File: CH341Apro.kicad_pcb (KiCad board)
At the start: 2 copper layers, 27.5 x 69 mm, 18 parts, among them J1 USB_A, J3 ZIF-16, J4 , J5 V_SEL, U1 AMS1117-3.3, U2 CH341a, Y1 12M

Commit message: Add JLCPCB assembly infos
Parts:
- removed R2: 0R, Resistor_SMD:R_0805_2012Metric
- removed REF**: WEEE-Logo_4.2x6mm_SilkScreen, Symbol:WEEE-Logo_4.2x6mm_SilkScreen
- added JP1: , Jumper:SolderJumper-2_P1.3mm_Open_Pad1.0x1.5mm, F.Cu at (109.2, 99.1)
- C5, C6: footprint Capacitor_SMD:C_0603_1608Metric -> Capacitor_SMD:C_0402_1005Metric
- R1: footprint Resistor_SMD:R_0805_2012Metric -> Resistor_SMD:R_0603_1608Metric
- Y1: footprint Crystal:Crystal_HC49-4H_Vertical -> Crystal:Crystal_SMD_5032-2Pin_5.0x3.2mm
- moved C6 2.87 mm to (114.2, 95.2), turned to 270 degrees
- moved C5 2.84 mm to (114.2, 87.0), turned to 90 degrees
- moved Y1 2.48 mm to (114.2, 91.2)
- moved R1 0.14 mm to (110.7, 105.5)
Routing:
- net /3V3: track 84.3 -> 89.5 mm
- net Net-(C3-Pad2): track 17.9 -> 14.1 mm
- net Net-(C5-Pad1): track 13.6 -> 10.2 mm
- net Net-(C6-Pad1): track 9.38 -> 6.58 mm
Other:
- rule pad_to_mask_clearance: 0.05 -> 0

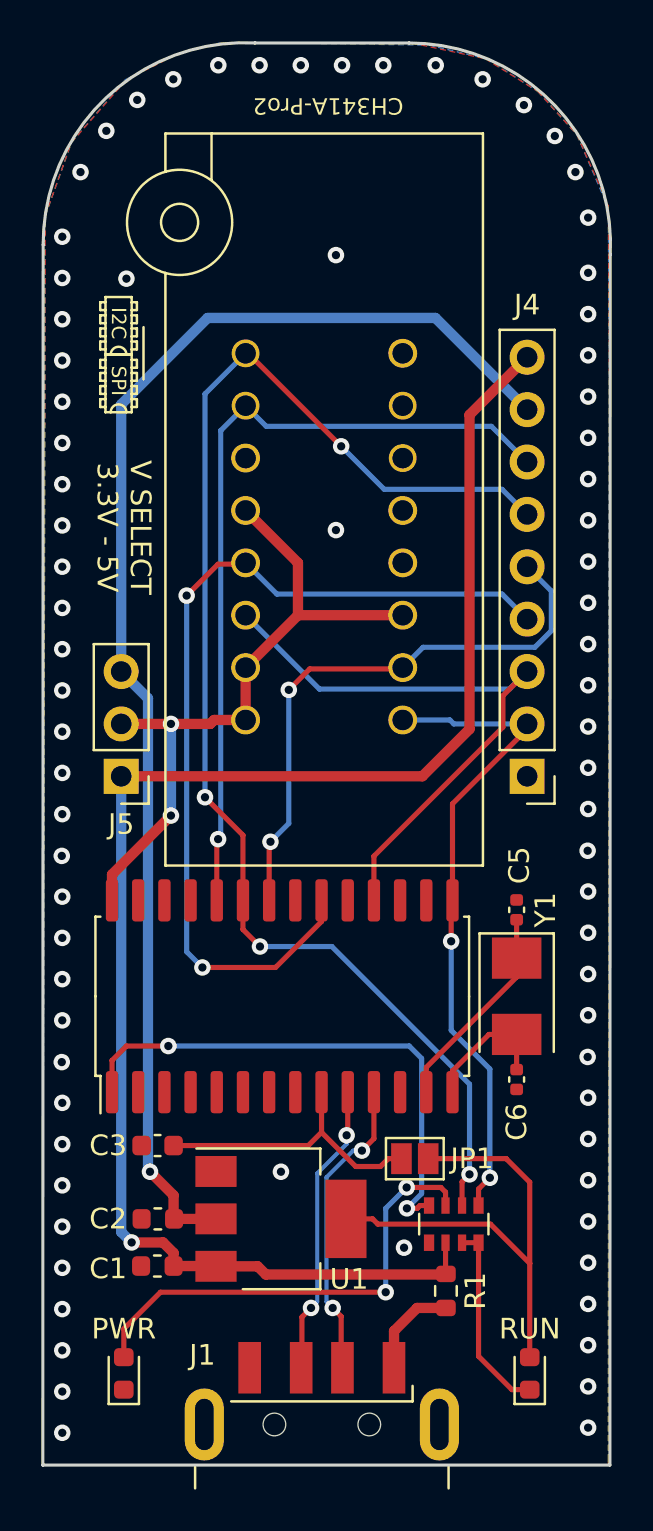
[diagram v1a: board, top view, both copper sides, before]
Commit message: Major ergo change
Updated components footprints for hand soldering.
Change VCC routing.
Add JP1/2 for selecting operating voltage.
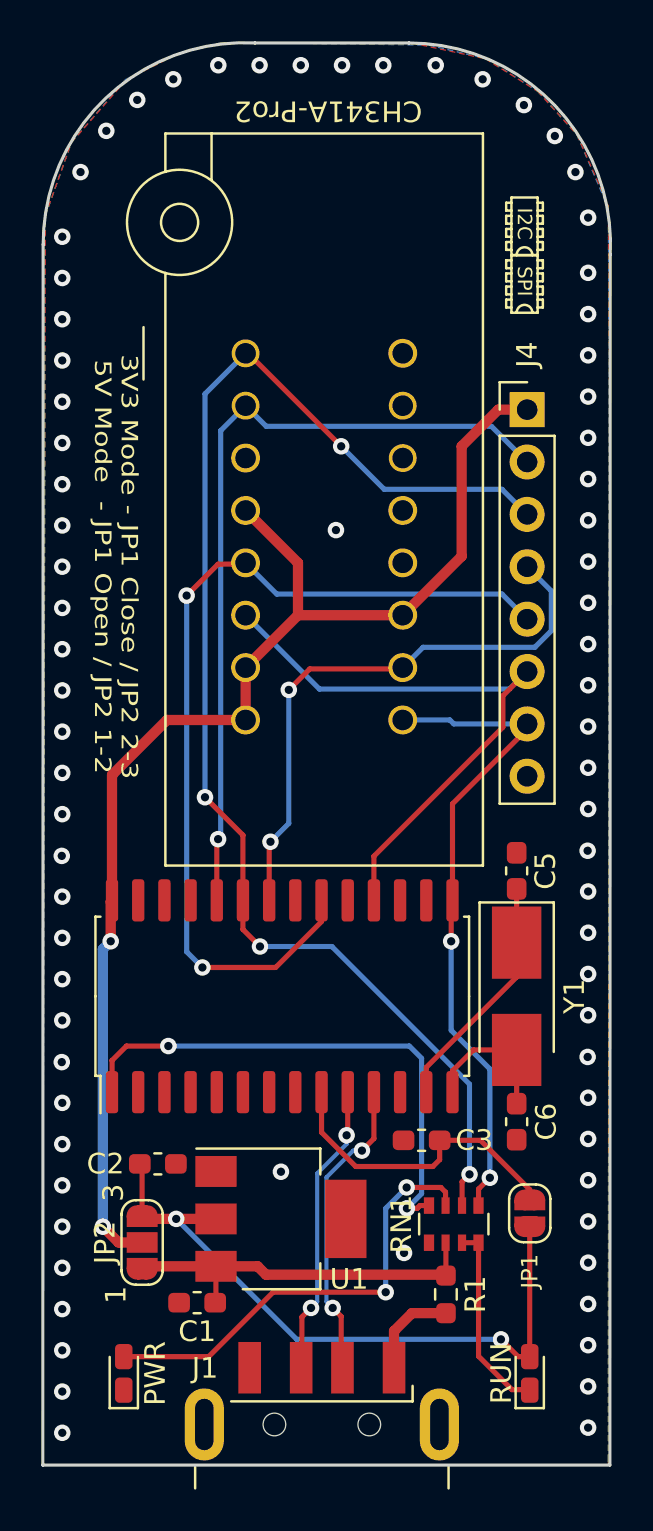
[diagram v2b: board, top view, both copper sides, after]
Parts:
- removed D1: PWR, LED_SMD:LED_0603_1608Metric
- removed D2: RUN, LED_SMD:LED_0603_1608Metric
- removed J5: V_SEL, Connector_PinHeader_2.54mm:PinHeader_1x03_P2.54mm_Vertical
- added JP2: V_SEL, Jumper:SolderJumper-3_P1.3mm_Open_RoundedPad1.0x1.5mm_NumberLabels, F.Cu at (96.0, 103.1)
- added PWR: PWR, LED_SMD:LED_0603_1608Metric_Castellated, F.Cu at (95.1, 109.5)
- added RUN: RUN, LED_SMD:LED_0603_1608Metric_Castellated, F.Cu at (114.8, 109.5)
- C1, C2, C3: footprint Capacitor_SMD:C_0603_1608Metric -> Capacitor_SMD:C_0603_1608Metric_Pad1.05x0.95mm_HandSolder
- C5, C6: footprint Capacitor_SMD:C_0402_1005Metric -> Capacitor_SMD:C_0603_1608Metric_Pad1.05x0.95mm_HandSolder
- J4: footprint Connector_PinHeader_2.54mm:PinHeader_1x09_P2.54mm_Vertical -> Connector_PinHeader_2.54mm:PinHeader_1x08_P2.54mm_Vertical
- JP1: footprint Jumper:SolderJumper-2_P1.3mm_Open_Pad1.0x1.5mm -> Jumper:SolderJumper-2_P1.3mm_Open_RoundedPad1.0x1.5mm
- R1: footprint Resistor_SMD:R_0603_1608Metric -> Resistor_SMD:R_0603_1608Metric_Pad0.98x0.95mm_HandSolder
- Y1: footprint Crystal:Crystal_SMD_5032-2Pin_5.0x3.2mm -> Crystal:Crystal_SMD_5032-2Pin_5.0x3.2mm_HandSoldering
- moved J4 17.8 mm to (114.7, 62.7), turned to 0 degrees
- moved C3 12.8 mm to (109.6, 98.2)
- moved JP1 6.17 mm to (114.8, 101.7), turned to 270 degrees
- moved C2 2.67 mm to (96.8, 99.3), turned to 0 degrees
- moved C1 2.62 mm to (98.7, 106.0)
- moved C6 2.05 mm to (114.2, 97.3)
- moved C5 1.89 mm to (114.2, 85.1)
- moved R1 0.17 mm to (110.7, 105.6)
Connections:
- J4 pad 1: Earth -> /VCC
- J4 pad 2: /CS -> /SCL
- J4 pad 3: /CLK -> /SDA
- J4 pad 4: /MOSI -> /MISO
- J4 pad 5: /MISO -> /MOSI
- J4 pad 6: /SDA -> /CLK
- J4 pad 7: /SCL -> /CS
- J4 pad 8: /3V3 -> Earth
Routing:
- net /5V: track 77.7 -> 18.4 mm, vias 1 -> 0
- net /3V3: track 89.5 -> 32.4 mm, vias 1 -> 2
- net /VCC: track 33.2 -> 62.5 mm
- net Net-(C5-Pad1): track 10.2 -> 13.5 mm
- net Net-(C6-Pad1): track 6.58 -> 8.88 mm
- net Net-(C3-Pad2): track 14.1 -> 15.3 mm
- net Net-(D1-Pad2): track 22.9 -> 22.1 mm
- net Earth: vias 79 -> 77
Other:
- board text added: "3V3 Mode - JP1 Close / JP2 2-3 5V Mode - JP1 Open / JP2 1-2"
- board text added: "VCC"
- board text removed: "3.3V"
- board text removed: "5V"
- board text removed: "V SELECT 3.3V - 5V"

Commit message: Changed drawing and placement
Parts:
- JP1: footprint Jumper:SolderJumper-2_P1.3mm_Open_RoundedPad1.0x1.5mm -> Connector_PinHeader_2.54mm:PinHeader_1x02_P2.54mm_Vertical
- JP2: footprint Jumper:SolderJumper-3_P1.3mm_Open_RoundedPad1.0x1.5mm_NumberLabels -> Connector_PinHeader_2.54mm:PinHeader_1x03_P2.54mm_Vertical
- moved PWR 65.5 mm to (158.0, 127.9)
- moved JP2 49.4 mm to (140.8, 123.8), turned to 180 degrees
- moved RUN 48.7 mm to (159.9, 127.9)
- moved RN1 48.2 mm to (155.8, 120.3)
- moved JP1 48.0 mm to (159.5, 119.3), turned to 0 degrees
- moved U1 48.0 mm to (147.6, 119.0)
- moved J1 48.0 mm to (149.6, 135.9)
- moved J3 48.0 mm to (145.9, 77.0)
- moved J4 48.0 mm to (159.5, 79.8)
- moved C2 48.0 mm to (141.6, 116.3)
- moved C5 48.0 mm to (159.0, 102.1)
- moved C6 48.0 mm to (159.0, 114.3)
- moved U2 48.0 mm to (147.6, 108.2)
- moved Y1 48.0 mm to (159.0, 108.2)
- moved C1 47.5 mm to (141.7, 126.2), turned to 0 degrees
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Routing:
- net Net-(D1-Pad2): track 22.1 -> 11.9 mm
- net Net-(C3-Pad2): track 15.3 -> 21.9 mm
- net Net-(RN1-Pad4): track 25.8 -> 22.6 mm
- net /5V: track 18.4 -> 20.8 mm
- net Net-(J1-Pad1): track 4.70 -> 2.44 mm
- net /SDA: track 66.5 -> 65.1 mm
- net /3V3: track 32.4 -> 33.2 mm
- net /VCC: track 62.5 -> 63.2 mm
- net /CS: track 32.0 -> 32.5 mm
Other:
- board text added: "1 2 3"
